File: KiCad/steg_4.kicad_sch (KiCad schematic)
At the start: 28 parts, among them U14 W65C02S

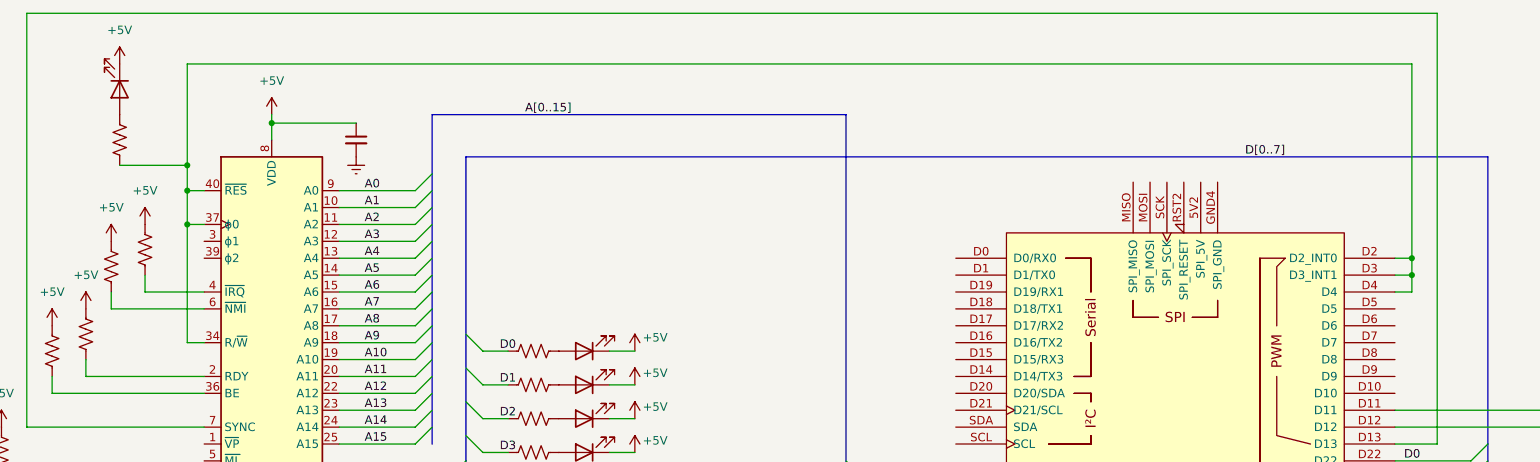
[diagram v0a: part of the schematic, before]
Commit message: Add trim potentiometer symbol and update power symbols in schematics
- Introduced a new trim potentiometer symbol (Device:R_Potentiometer_Trim) with properties for reference, value, footprint, and simulation details.
- Updated existing power symbols for +5V and Earth, including new references and descriptions.
- Adjusted positions and properties of various components in the schematic to enhance clarity and organization.
- Updated multiple schematic images to reflect the latest changes.
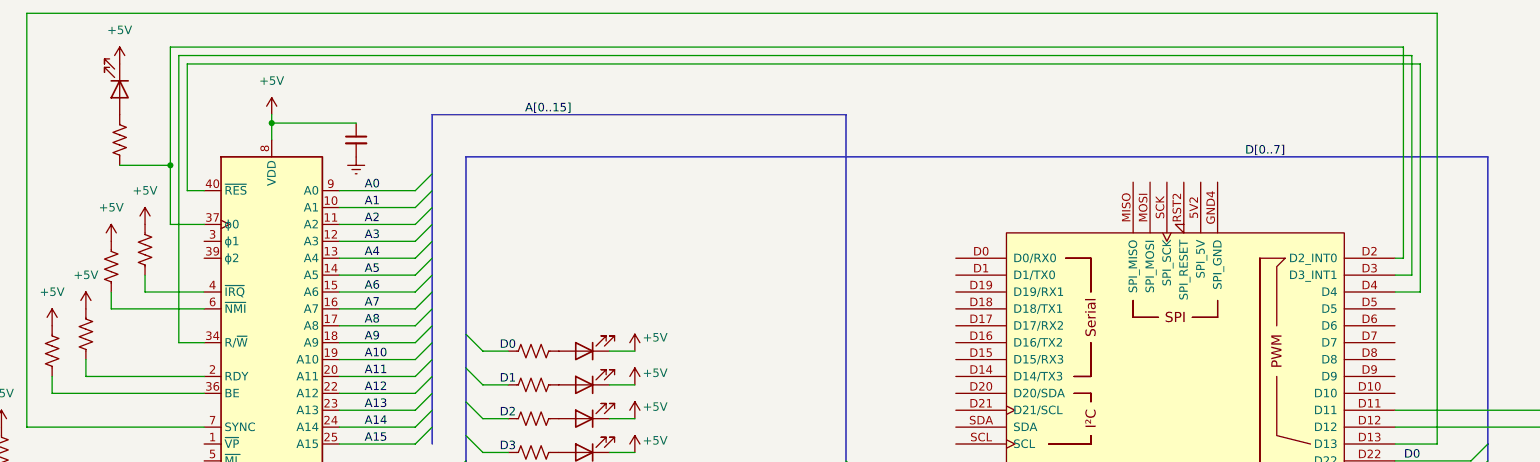
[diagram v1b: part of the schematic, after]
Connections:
- new net: A8.D2 (D2_INT0), R53.2, U14.37 (ϕ0)
- new net: A8.D3 (D3_INT1), U14.34 (R/~{W})
- new net: A8.D4, U14.40 (~{RES})

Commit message: Revert "Add trim potentiometer symbol and update power symbols in schematics"
This reverts commit c4bb345892a428583a00d61d4c040ffcc3a1eb40.
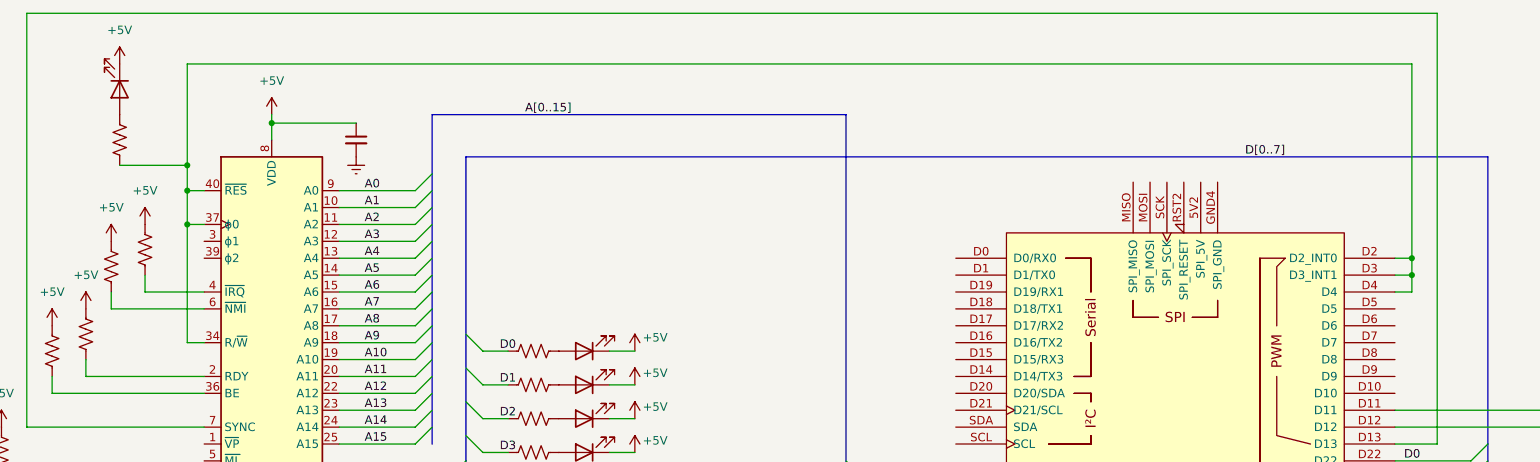
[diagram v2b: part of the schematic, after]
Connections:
- net at A8.D2 (D2_INT0), R53.2, U14.37 (ϕ0): now also A8.D3 (D3_INT1), A8.D4, U14.34 (R/~{W}), U14.40 (~{RES})
